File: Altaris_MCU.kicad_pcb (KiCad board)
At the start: 4 copper layers, 101.1 x 69.8 mm, 62 parts, among them J1 Screw_Terminal_01x02, J11 Screw_Terminal_01x02, J12 Screw_Terminal_01x02, J2 Conn_01x04_Pin, J3 Screw_Terminal_01x02, J4 Screw_Terminal_01x02, J5 Conn_01x04_Pin, J6 Conn_01x04_Pin, J9 USB_C_Receptacle_USB2.0_16P, SW2 RESET1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

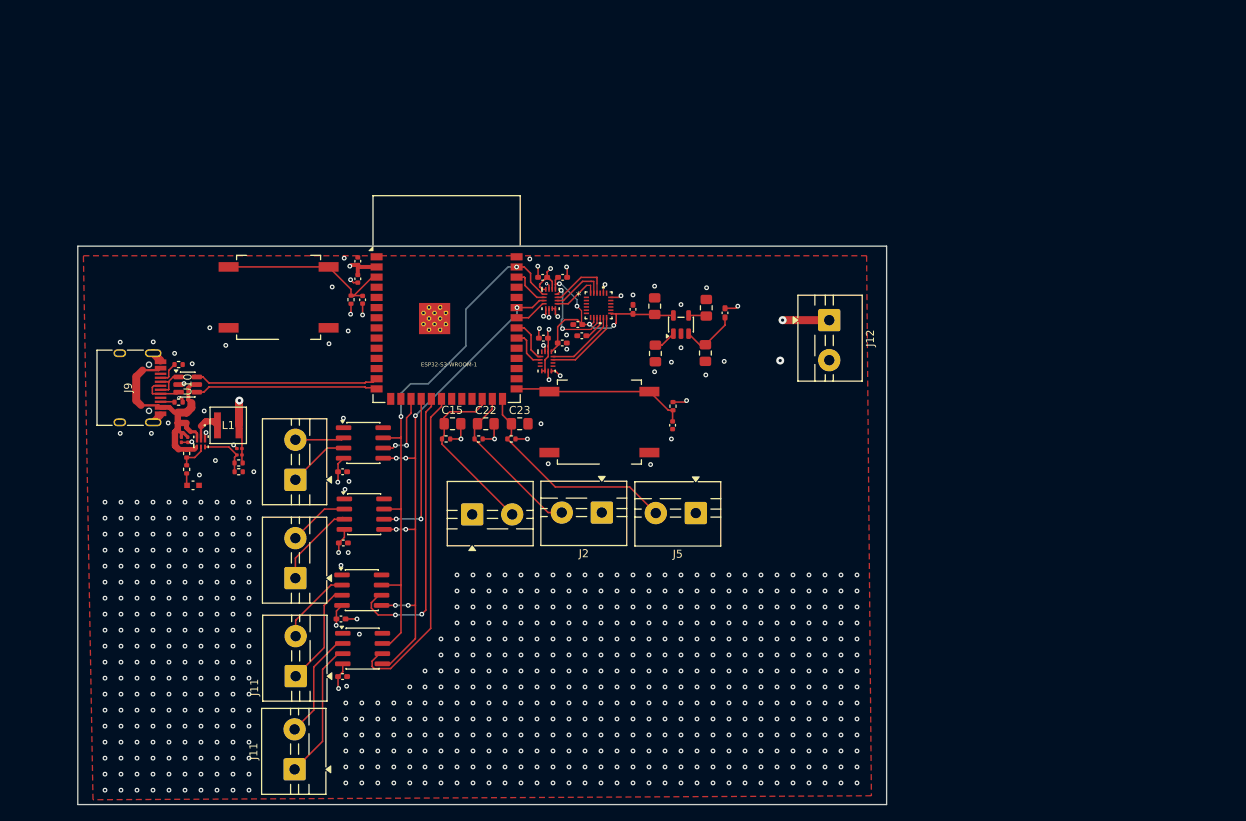
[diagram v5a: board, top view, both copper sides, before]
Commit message: added two screw terminal and MAX for extra thermocouples
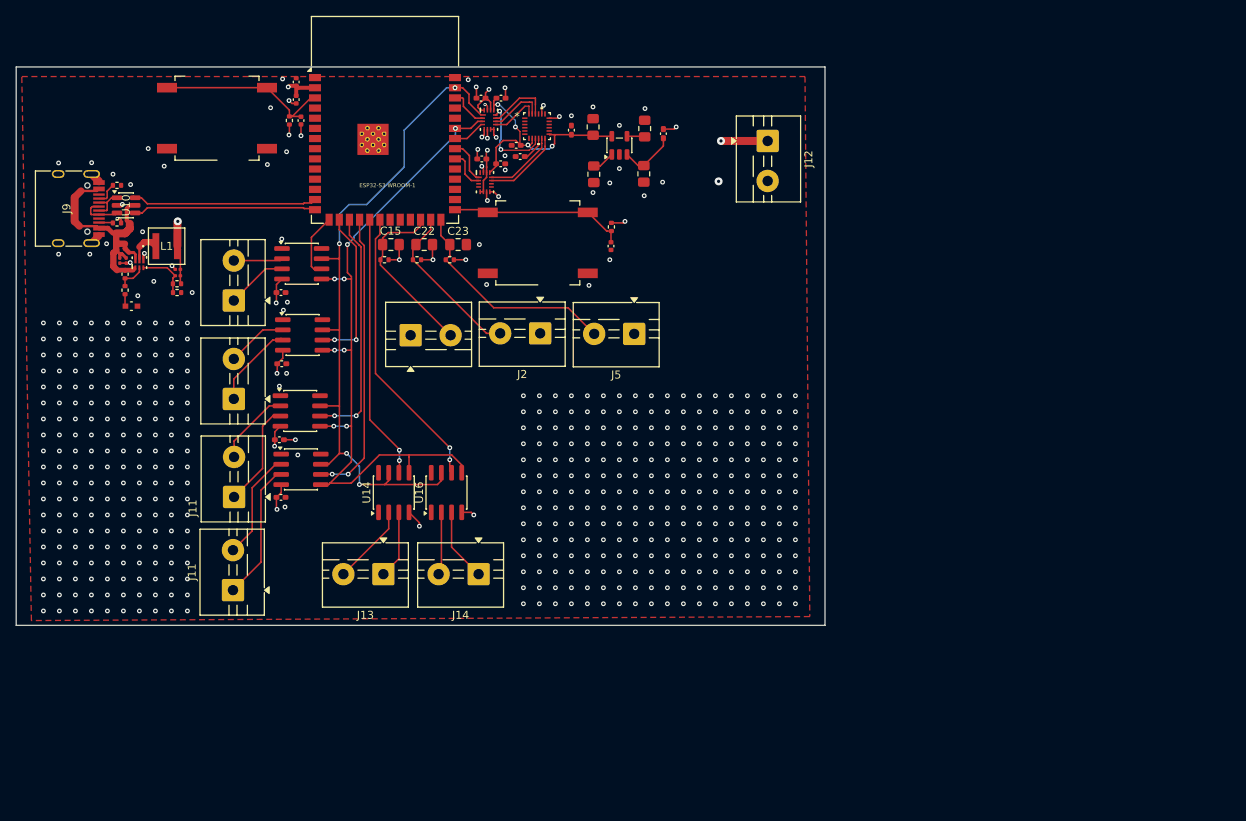
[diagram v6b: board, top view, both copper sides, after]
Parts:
- added J13: Screw_Terminal_01x02, TerminalBlock:TerminalBlock_MaiXu_MX126-5.0-02P_1x02_P5.00mm, F.Cu at (146.6, 131.1)
- added J14: Screw_Terminal_01x02, TerminalBlock:TerminalBlock_MaiXu_MX126-5.0-02P_1x02_P5.00mm, F.Cu at (158.5, 131.1)
- added U14: MAX31855KASA, Package_SO:SOIC-8_3.9x4.9mm_P1.27mm, F.Cu at (147.9, 120.9)
- added U16: MAX31855KASA, Package_SO:SOIC-8_3.9x4.9mm_P1.27mm, F.Cu at (154.5, 120.9)
- moved C11 23.7 mm to (170.1, 75.6)
- moved C12 23.7 mm to (163.2, 77.5)
- moved C2 23.7 mm to (135.7, 69.6)
- moved C3 23.7 mm to (135.7, 71.8)
- moved FB2 23.7 mm to (181.6, 76.0)
- moved J2 23.7 mm to (166.2, 101.0)
- moved J5 23.7 mm to (177.9, 101.1)
- moved R9 23.7 mm to (134.8, 74.4)
- moved U5 23.7 mm to (176.1, 77.5)
- moved J11 23.7 mm to (127.8, 133.1)
- moved L1 23.7 mm to (119.5, 90.1)
- moved LED1 23.7 mm to (115.1, 97.6)
- moved R11 23.7 mm to (114.3, 95.6)
- moved R5 23.7 mm to (113.3, 82.5)
- moved R6 23.7 mm to (114.3, 93.6)
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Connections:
- U1 pad 15: unconnected-(U1-IO3-Pad15) -> MAX_CS1
- U1 pad 16: unconnected-(U1-IO46-Pad16) -> MAX_CS2
- U1 pad 17: MAX_CS1 -> MAX_CS3
- U1 pad 18: MAX_CS2 -> MAX_CS4
- U1 pad 19: MAX_CS3 -> MAX_CS5
- U1 pad 20: MAX_CS4 -> MAX_CS6
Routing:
- net MAX_CS6: track 0.00 -> 35.8 mm, vias 0 -> 2
- net MAX_CS5: track 0.00 -> 33.2 mm, vias 0 -> 2
- net CLK: track 68.1 -> 89.2 mm
- net MISO: track 68.6 -> 87.2 mm, vias 2 -> 4
- net T5-: track 0.00 -> 10.1 mm
- net T6+: track 0.00 -> 9.13 mm
- net T5+: track 0.00 -> 8.53 mm
- net T6-: track 0.00 -> 7.87 mm
- net MAX_CS3: track 36.4 -> 30.3 mm
- net MAX_CS4: track 41.8 -> 37.4 mm, vias 0 -> 2
- net +3.3V_b: track 50.2 -> 54.1 mm, vias 14 -> 16
- net MAX_CS1: track 9.16 -> 8.21 mm, vias 2 -> 0
- net GND: vias 665 -> 504

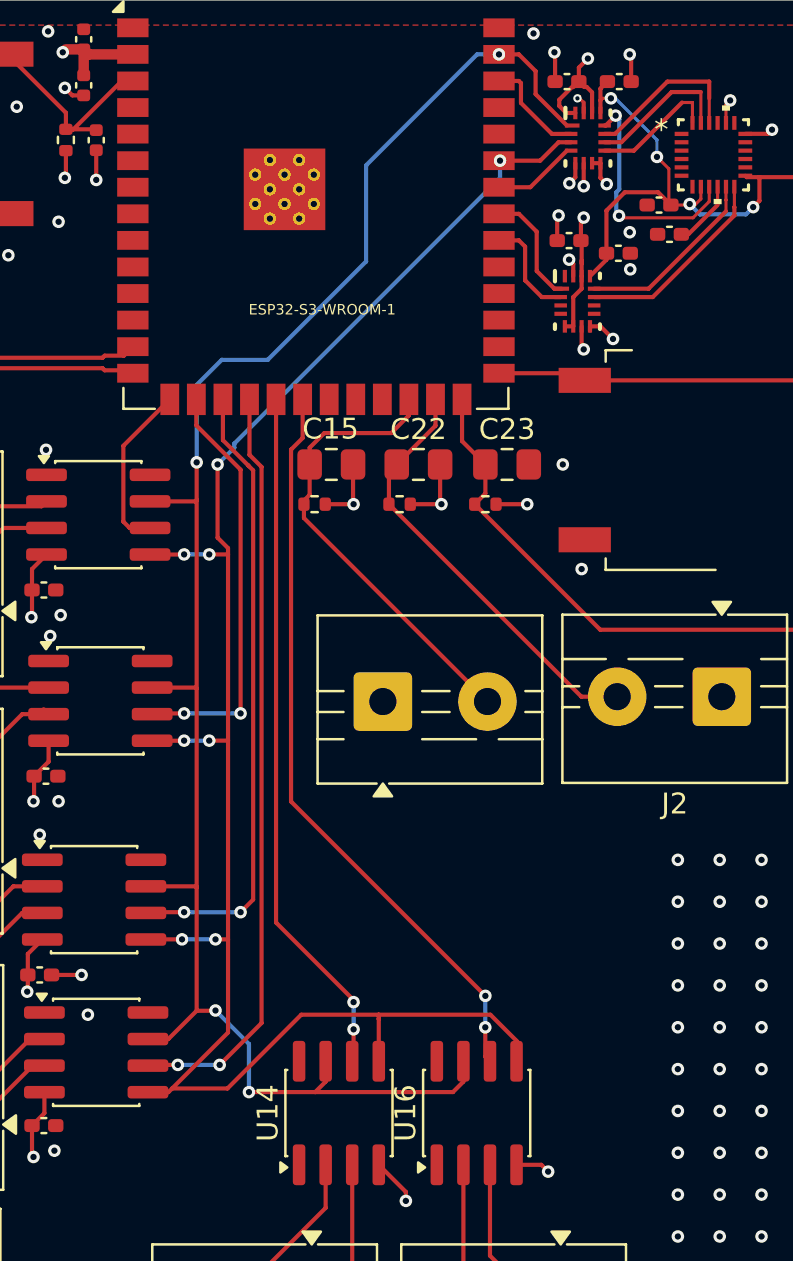
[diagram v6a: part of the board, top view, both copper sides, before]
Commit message: Added header for MicroSD module to layout, changed 3 thermocouple MAX to T type in schematic only
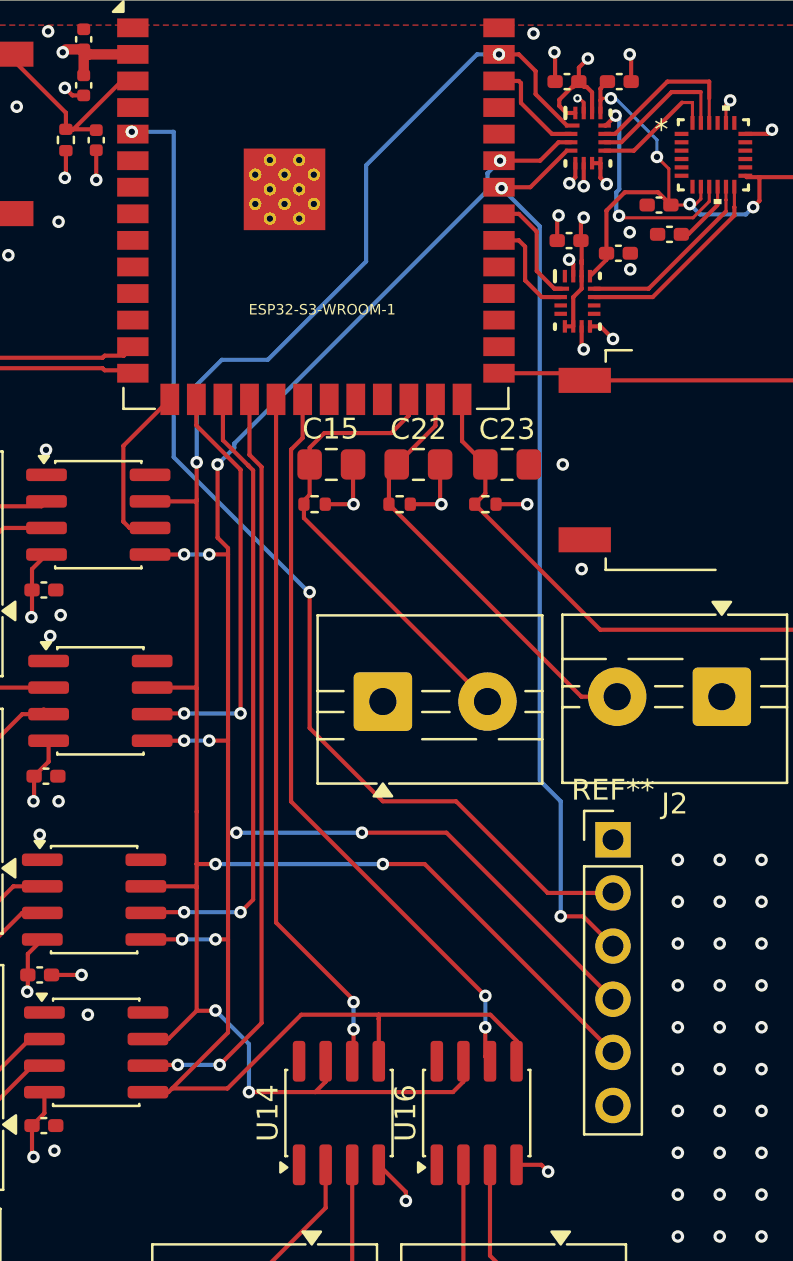
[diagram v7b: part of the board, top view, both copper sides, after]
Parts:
- added REF**: PinHeader_1x06_P2.54mm_Vertical, Connector_PinHeader_2.54mm:PinHeader_1x06_P2.54mm_Vertical, F.Cu at (161.0, 107.8)
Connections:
- U1 pad 5: unconnected-(U1-IO5-Pad5) -> SD_CS
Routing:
- net SD_CS: track 0.00 -> 51.1 mm, vias 0 -> 2
- net MOSI: track 3.97 -> 43.0 mm, vias 0 -> 2
- net MISO: track 87.2 -> 110.8 mm, vias 4 -> 8
- net CLK: track 89.2 -> 111.2 mm, vias 8 -> 11
- net GND: vias 504 -> 501

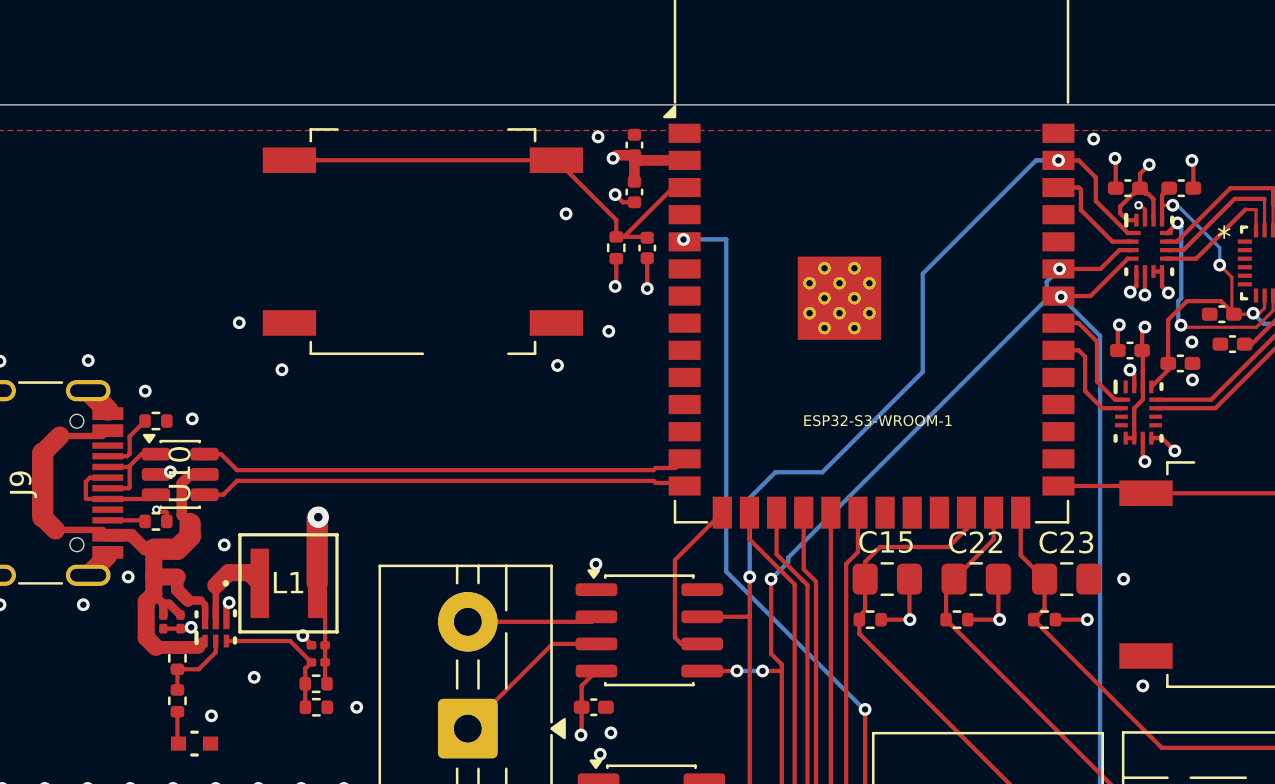
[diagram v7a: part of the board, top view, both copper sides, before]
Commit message: added vias, tweaked sd_cs via/tracing
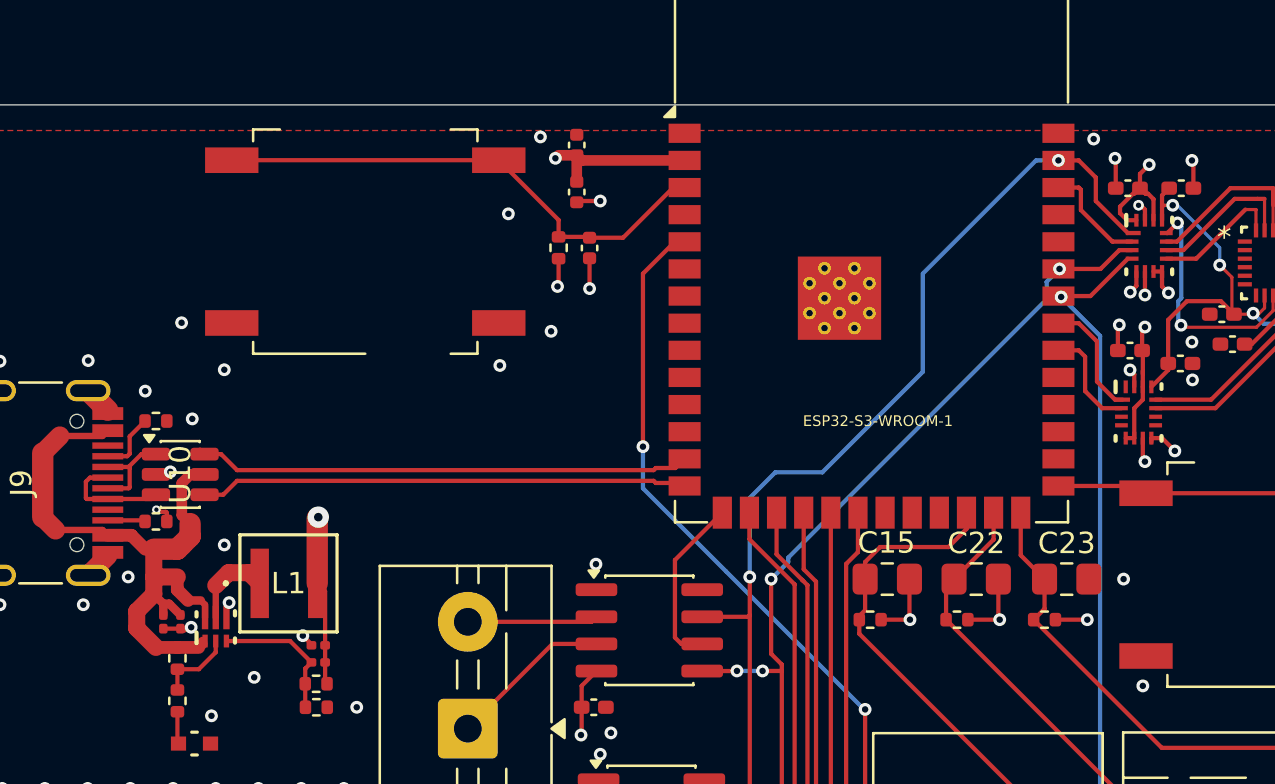
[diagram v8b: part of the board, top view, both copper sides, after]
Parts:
- moved C18 2.70 mm to (133.6, 74.4)
- moved SW2 2.70 mm to (123.1, 74.1)
- moved C2 2.70 mm to (133.0, 69.6)
- moved C3 2.70 mm to (133.0, 71.8)
- moved R9 2.70 mm to (132.2, 74.4)
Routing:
- net +3.3V_b: track 54.1 -> 56.8 mm
- net ESP32_EN: track 22.9 -> 24.5 mm
- net SD_CS: track 51.1 -> 51.7 mm
- net GND: track 32.8 -> 32.9 mm, vias 501 -> 504
- net MISO: vias 8 -> 6
- net CLK: vias 11 -> 10
